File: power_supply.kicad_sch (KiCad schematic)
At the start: 35 parts, among them J4 tp5100, J5 BATTERY, J8 GSB1C411111DS1HR, U2 TPS63000, U4 TPS63000

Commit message: -add some changes to power section and display
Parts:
- added IC2: TPS2113ADRBR, lib:SON65P300X300X100-9N-D, symbol TPS2113ADRBR:TPS2113ADRBR
- added J2: wireless_charging, Connector_PinHeader_2.54mm:PinHeader_1x02_P2.54mm_Horizontal, symbol Connector:Conn_01x02_Pin
- added R34, R35, R36: R, Resistor_SMD:R_0603_1608Metric_Pad0.98x0.95mm_HandSolder, symbol Device:R
- added SW2: REG_EN, Button_Switch_THT:SW_Slide_SPDT_Angled_CK_OS102011MA1Q, symbol Switch:SW_SPST
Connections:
- net +BATT: now also J4.4 (Pin_4); no longer J4.1 (Pin_1)
- net GND: now also J4.1 (Pin_1), J4.3 (Pin_3), IC2.2 (~{EN}), IC2.5 (GND_1), IC2.9 (GND_2), J2.2 (Pin_2), R34.2, R36.2, SW2.2 (B); no longer J4.2 (Pin_2), J4.4 (Pin_4)
- net VBUS: now also J4.2 (Pin_2), IC2.7 (OUT); no longer J4.3 (Pin_3), J8.A4B9 (VBUS_A), J8.B4A9 (VBUS_B)
- net REG_EN: now reaches R6.2, R7.1, U2.6 (EN)
- net REG_EN: now also R19.2, R20.1, U4.6 (EN), SW2.1 (A)
- new net: IC2.3 (VSNS), R34.1, R35.2
- new net: IC2.4 (ILIM), R36.1
- new net Charger_plugged_in?: IC2.1 (STAT)
- new net VBUS_QI: IC2.8 (IN1), J2.1 (Pin_1), R35.1
- new net VBUS_USB: IC2.6 (IN2), J8.A4B9 (VBUS_A), J8.B4A9 (VBUS_B)
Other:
- note added: "On/Off switch"

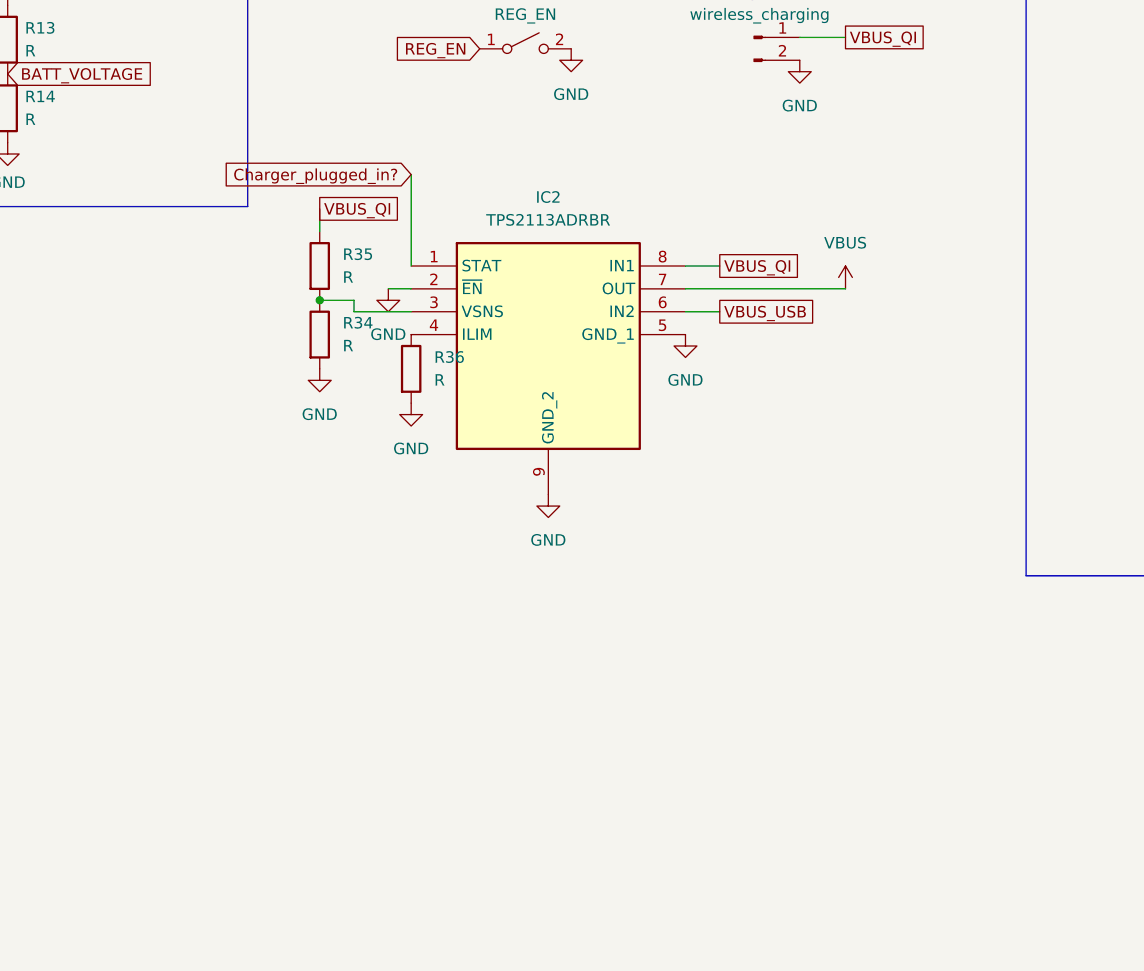
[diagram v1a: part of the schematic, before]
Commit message: -add soft latching circuit, routing mostly done
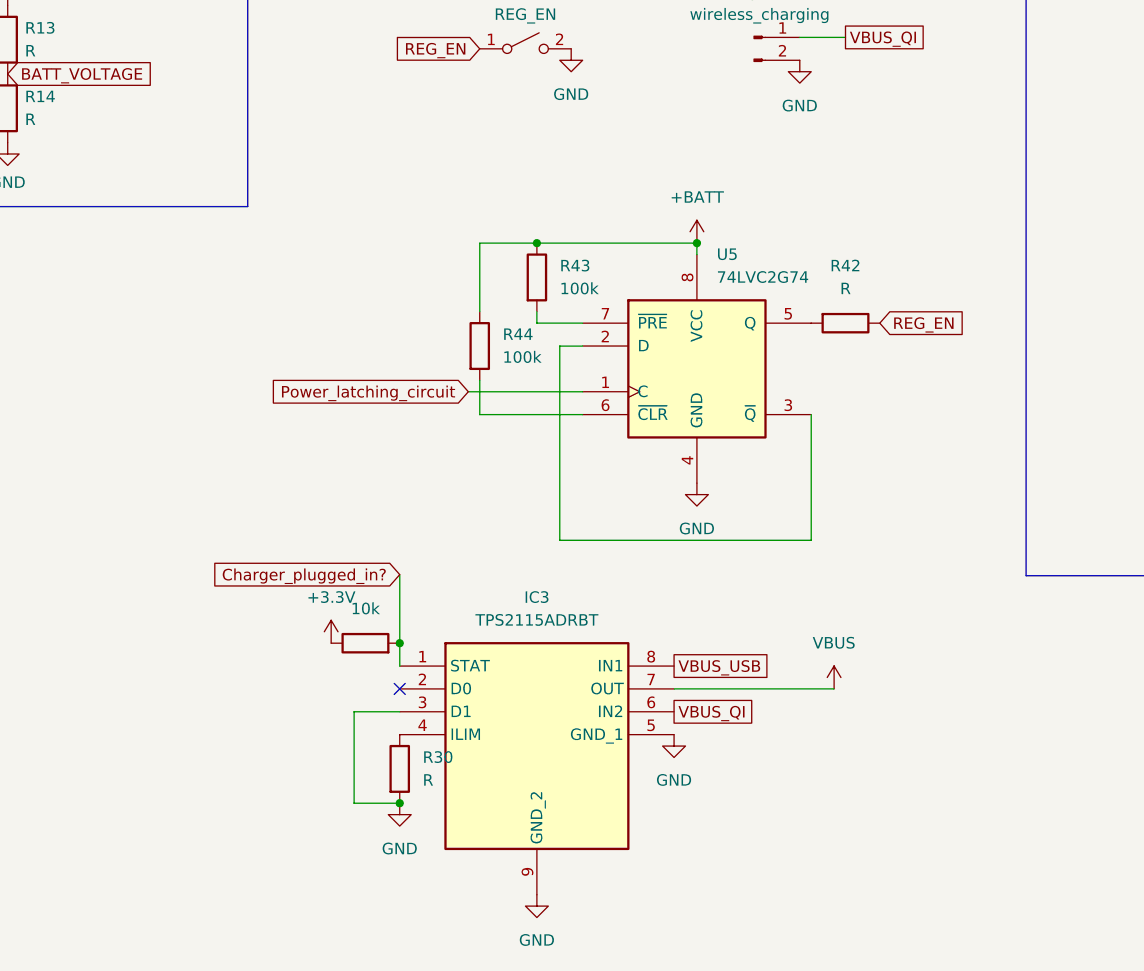
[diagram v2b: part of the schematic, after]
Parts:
- removed IC2: TPS2113ADRBR, lib:SON65P300X300X100-9N-D, symbol TPS2113ADRBR:TPS2113ADRBR
- removed R34, R35, R36: R, Resistor_SMD:R_0603_1608Metric_Pad0.98x0.95mm_HandSolder, symbol Device:R
- added IC3: TPS2115ADRBT, lib:SON65P300X300X100-9N-D, symbol TPS2115ADRBT:TPS2115ADRBT
- added R29: 10k, Resistor_SMD:R_0603_1608Metric_Pad0.98x0.95mm_HandSolder, symbol Device:R
- added R30, R42: R, Resistor_SMD:R_0603_1608Metric_Pad0.98x0.95mm_HandSolder, symbol Device:R
- added R43, R44: 100k, Resistor_SMD:R_0603_1608Metric_Pad0.98x0.95mm_HandSolder, symbol Device:R
- added U5: 74LVC2G74, Package_SO:TSSOP-8_3x3mm_P0.65mm, symbol 74xGxx:74LVC2G74
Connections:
- net +3.3V: now also R29.1
- net +BATT: now also R43.1, R44.1, U5.8 (VCC)
- net Charger_plugged_in?: now also IC3.1 (STAT), R29.2
- net GND: now also IC3.3 (D1), IC3.5 (GND_1), IC3.9 (GND_2), R30.2, U5.4 (GND)
- net REG_EN: now also R42.1
- net VBUS: now also IC3.7 (OUT)
- net VBUS_QI: now also IC3.6 (IN2)
- net VBUS_USB: now also IC3.8 (IN1)
- new net: IC3.4 (ILIM), R30.1
- new net: R42.2, U5.5 (Q)
- new net: R43.2, U5.7 (~{PRE})
- new net: U5.2 (D), U5.3 (~{Q})
- new net: R44.2, U5.6 (~{CLR})
- new net Power_latching_circuit: U5.1 (C)
- no-connect marks 2 -> 3

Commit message: -add end revision
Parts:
- added C24: 100n, Capacitor_SMD:C_0603_1608Metric_Pad1.08x0.95mm_HandSolder, symbol Device:C
- added U7: USBLC6-2P6, Package_TO_SOT_SMD:SOT-666, symbol Power_Protection:USBLC6-2P6
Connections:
- net D+: now also U7.6 (I/O1); no longer J8.A6 (D1+), J8.B6 (D2+)
- net D-: now also U7.4 (I/O2); no longer J8.A7 (D1-), J8.B7 (D2-)
- net GND: now also C24.2, U7.2 (GND)
- net VBUS_USB: now also C24.1, U7.5 (VBUS)
- new net D+_IN: J8.A6 (D1+), J8.B6 (D2+), U7.1 (I/O1)
- new net D-_IN: J8.A7 (D1-), J8.B7 (D2-), U7.3 (I/O2)
